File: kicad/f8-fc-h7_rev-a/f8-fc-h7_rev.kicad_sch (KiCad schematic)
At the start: 65 parts, among them J10 USART1, J11 USART2, J12 FC-ESC con, J14 UART4, J15 USART6, J16 I2C, J17 I2C, J18 I2C, J19 Debug, SW1 SW_SPST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

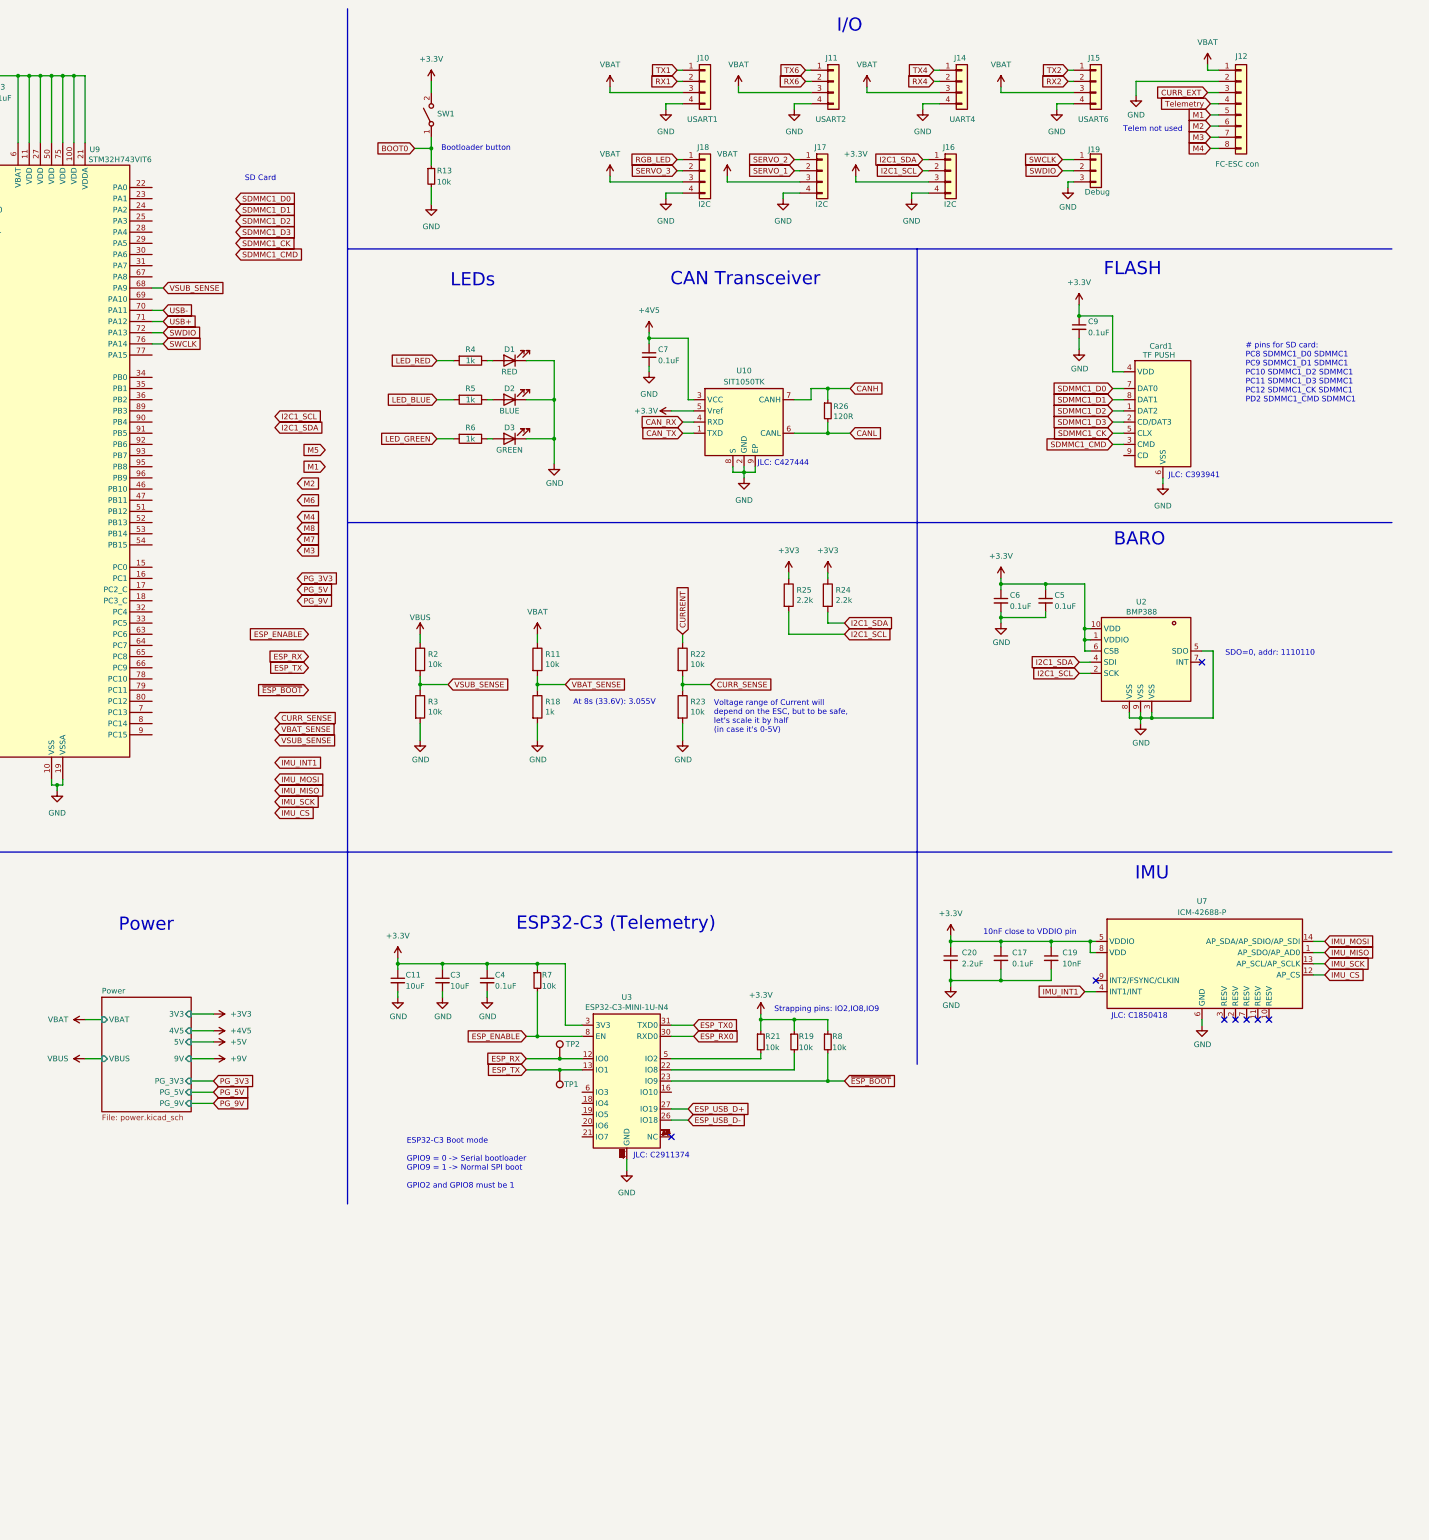
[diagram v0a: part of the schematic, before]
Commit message: Initial ethernet PHY support
Realized however that the IC chosen (DP83848TSQ/NOPB) which
pixhawk uses in their example in Bus standard 6, isn't supported by Ardupilot.
So should probably change IC
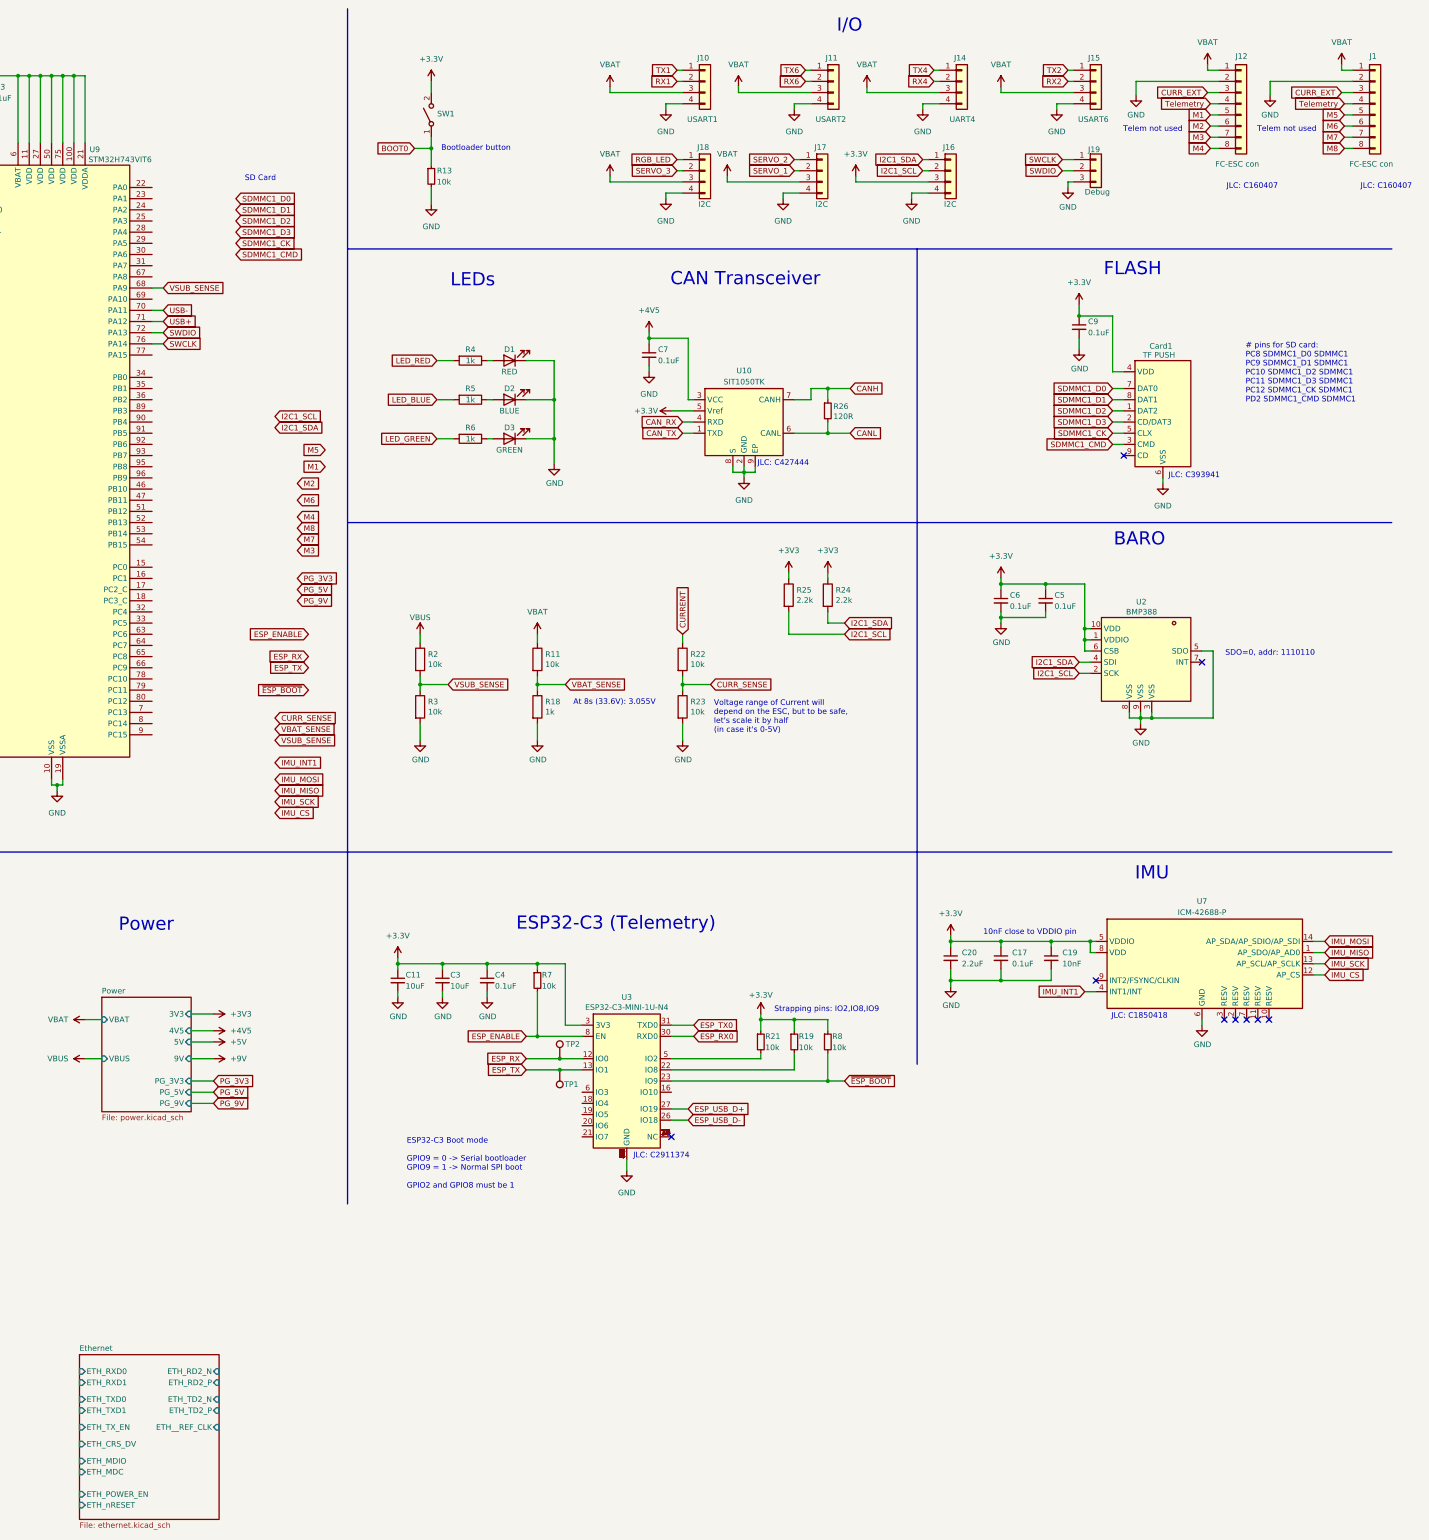
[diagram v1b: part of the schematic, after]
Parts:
- added J1: FC-ESC con, easyeda2kicad:CONN-TH_SM08B-SRSS-TB-LF-SN, symbol Connector_Generic:Conn_01x08
- J12: footprint custom:Conn_8_Accesory -> easyeda2kicad:CONN-TH_SM08B-SRSS-TB-LF-SN; LSCS Part (none) -> C160407
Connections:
- net CURR_EXT: now also J1.3 (Pin_3)
- net GND: now also J1.2 (Pin_2)
- net M5: now also J1.5 (Pin_5)
- net M6: now also J1.6 (Pin_6)
- net M7: now also J1.7 (Pin_7)
- net M8: now also J1.8 (Pin_8)
- net Telemetry: now also J1.4 (Pin_4)
- net VBAT: now also J1.1 (Pin_1)
- no-connect marks 11 -> 12
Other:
- added sheet Ethernet (ethernet.kicad_sch)
- note added: "JLC: C160407"

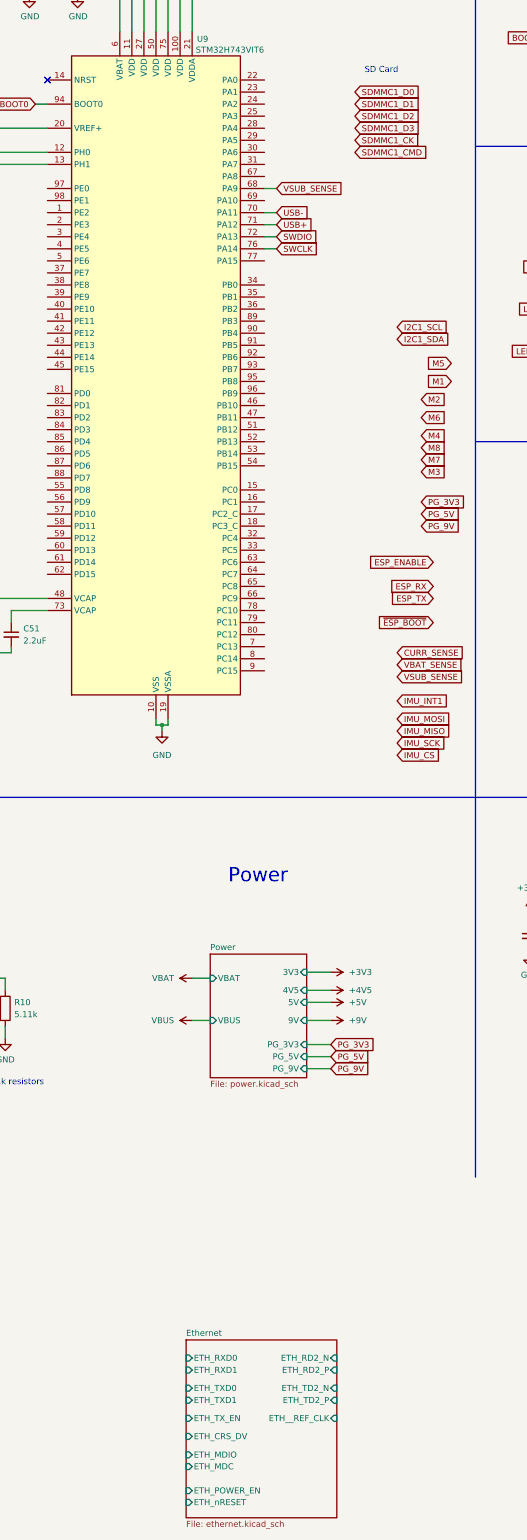
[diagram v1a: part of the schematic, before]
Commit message: Swapped to LAN8742 Ethernet PHY
This was is supported by AP so seems more safe
to use this.
Also seems a bit simpler in wiring as it has a few less pins.
A downside is that I cannot find a proper application
schematic example online..
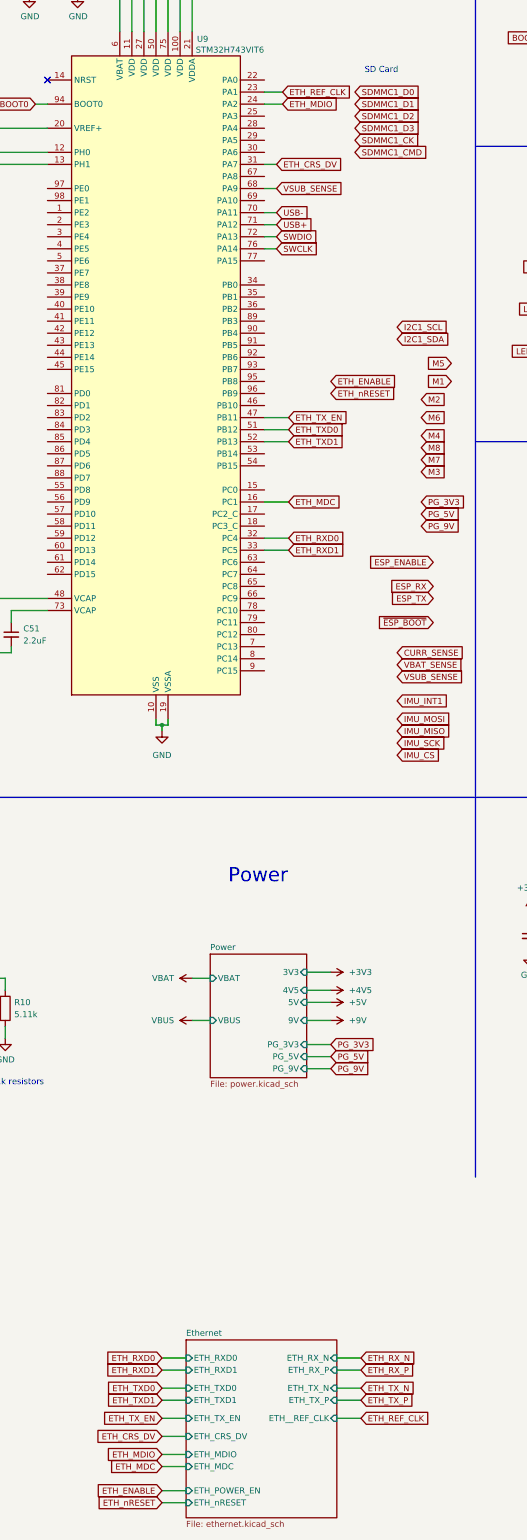
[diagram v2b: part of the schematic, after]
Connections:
- net ETH_MDC: now reaches U9.16 (PC1)
- net ETH_REF_CLK: now reaches U9.23 (PA1)
- net ETH_MDIO: now reaches U9.24 (PA2)
- net ETH_CRS_DV: now reaches U9.31 (PA7)
- net ETH_RXD0: now reaches U9.32 (PC4)
- net ETH_RXD1: now reaches U9.33 (PC5)
- net ETH_TX_EN: now reaches U9.47 (PB11)
- net ETH_TXD0: now reaches U9.51 (PB12)
- net ETH_TXD1: now reaches U9.52 (PB13)
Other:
- sheet Ethernet ports: added ETH_RX_N, ETH_RX_P, ETH_TX_N, ETH_TX_P; removed ETH_RD2_N, ETH_RD2_P, ETH_TD2_N, ETH_TD2_P
